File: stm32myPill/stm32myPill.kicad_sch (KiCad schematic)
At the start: 10 parts

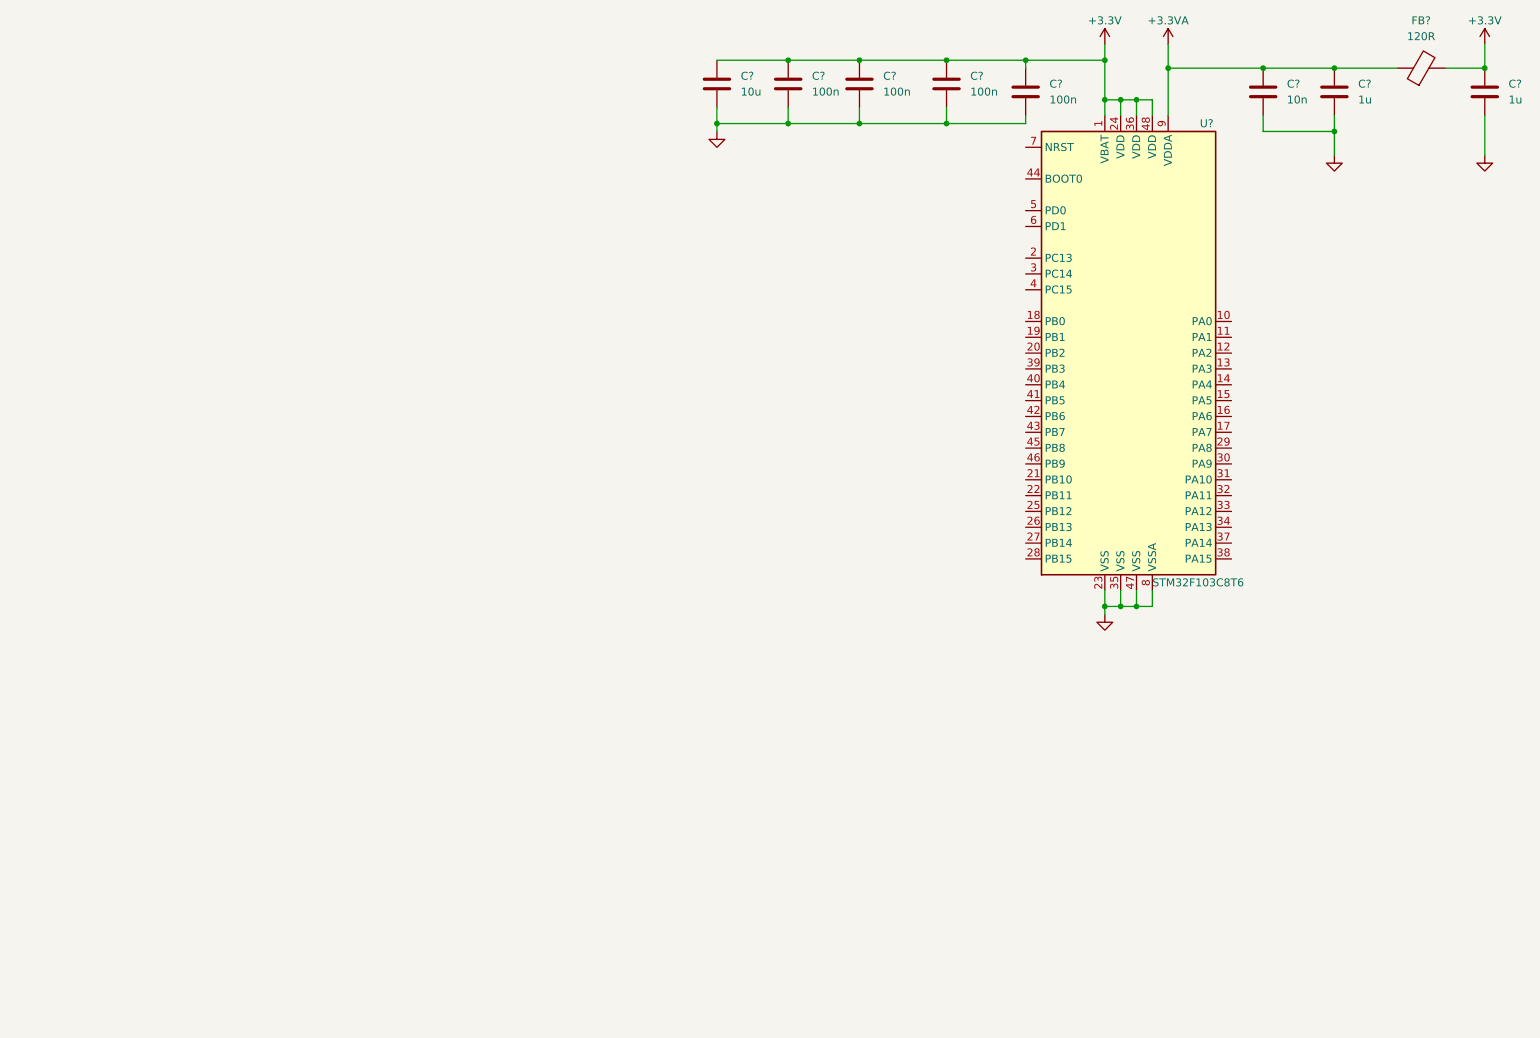
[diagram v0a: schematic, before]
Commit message: added CubeIDE and finished MCU schematic
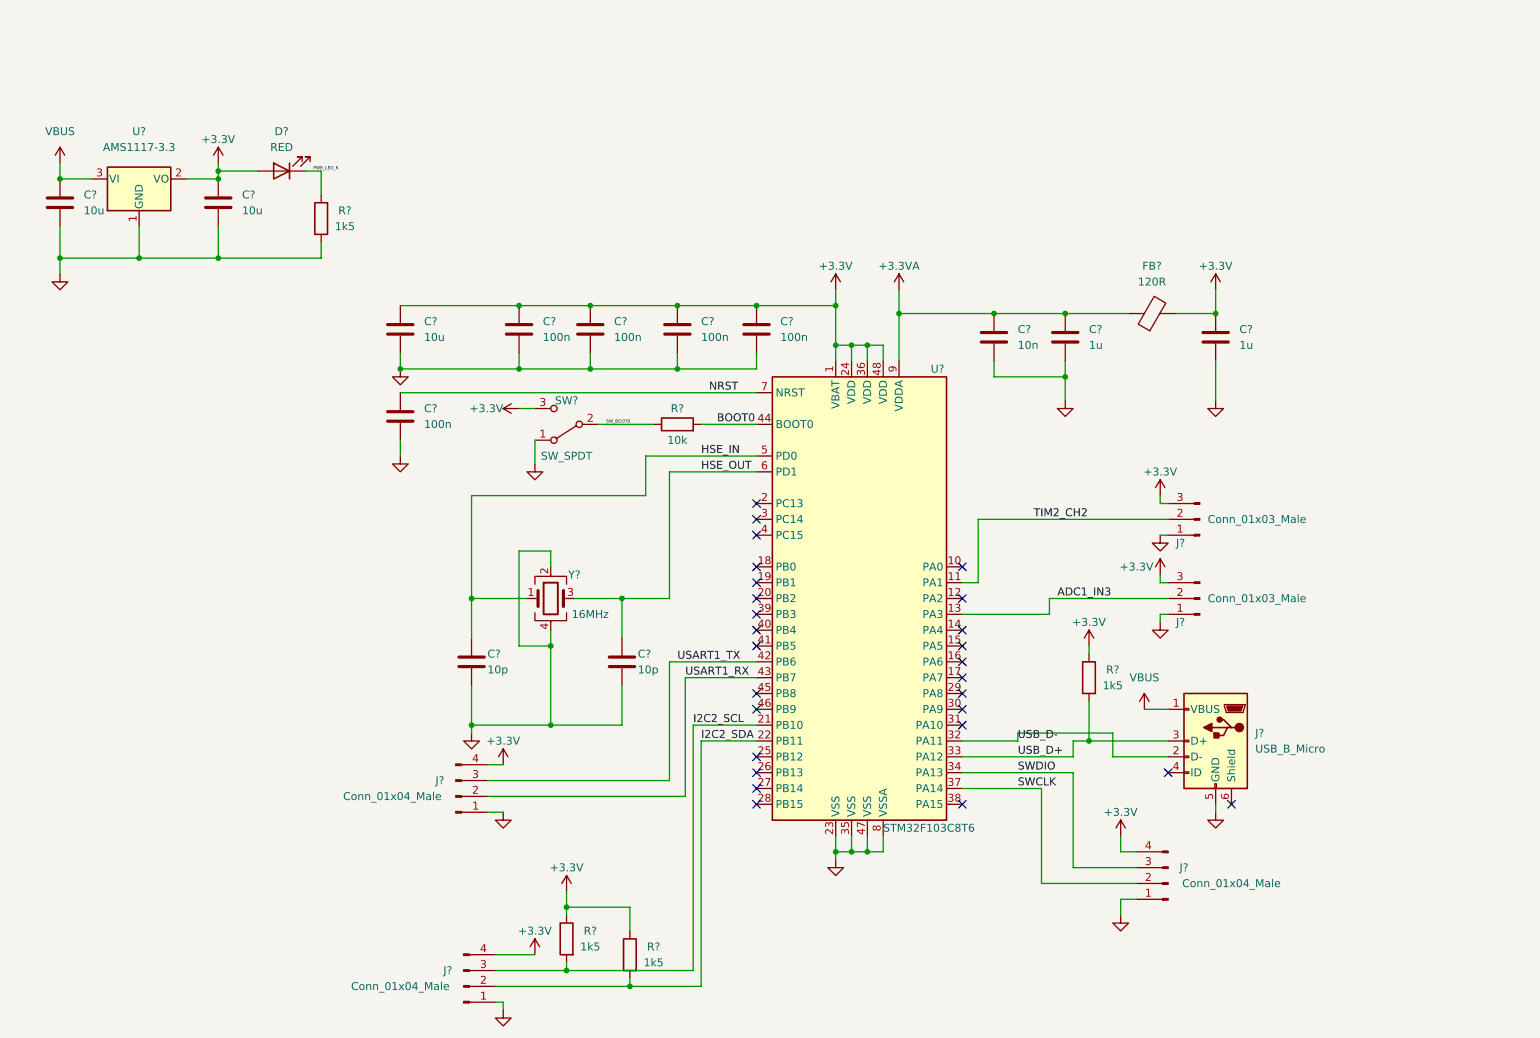
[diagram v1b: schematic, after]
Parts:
- added C? (x2): 10p, symbol Device:C
- added C? (x2): 10u, symbol Device:C
- added C?: 100n, symbol Device:C
- added D?: RED, symbol Device:LED
- added J? (x3): Conn_01x04_Male, symbol Connector:Conn_01x04_Male
- added J? (x2): Conn_01x03_Male, symbol Connector:Conn_01x03_Male
- added J?: USB_B_Micro, symbol Connector:USB_B_Micro
- added R? (x4): 1k5, symbol Device:R
- added R?: 10k, symbol Device:R
- added SW?: SW_SPDT, symbol Switch:SW_SPDT
- added U?: AMS1117-3.3, Package_TO_SOT_SMD:SOT-223-3_TabPin2, symbol Regulator_Linear:AMS1117-3.3
- added Y?: 16MHz, symbol Device:Crystal_GND24
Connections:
- net +3V3: now also C?.1, D?.2 (A), J?.3 (Pin_3), J?.3 (Pin_3), J?.4 (Pin_4), J?.4 (Pin_4), J?.4 (Pin_4), R?.1, R?.1, R?.1, SW?.3 (C), U?.2 (VO)
- net GND: now also C?.2, C?.2, C?.2, C?.2, C?.2, J?.1 (Pin_1), J?.1 (Pin_1), J?.1 (Pin_1), J?.1 (Pin_1), J?.1 (Pin_1), J?.5 (GND), R?.1, SW?.1 (A), U?.1 (GND), Y?.2, Y?.4
- net TIM2_CH2: now reaches U?.11 (PA1)
- net TIM2_CH2: now also J?.2 (Pin_2)
- net ADC1_IN3: now reaches U?.13 (PA3)
- net ADC1_IN3: now also J?.2 (Pin_2)
- net I2C2_SCL: now reaches U?.21 (PB10)
- net I2C2_SCL: now also J?.3 (Pin_3), R?.2
- net I2C2_SDA: now reaches U?.22 (PB11)
- net I2C2_SDA: now also J?.2 (Pin_2), R?.2
- net USB_D-: now reaches U?.32 (PA11)
- net USB_D-: now also J?.2 (D-)
- net USB_D+: now reaches U?.33 (PA12)
- net USB_D+: now also J?.3 (D+), R?.2
- net SWDIO: now reaches U?.34 (PA13)
- net SWDIO: now also J?.3 (Pin_3)
- net SWCLK: now reaches U?.37 (PA14)
- net SWCLK: now also J?.2 (Pin_2)
- net USART1_TX: now reaches U?.42 (PB6)
- net USART1_TX: now also J?.3 (Pin_3)
- net USART1_RX: now reaches U?.43 (PB7)
- net USART1_RX: now also J?.2 (Pin_2)
- net BOOT0: now reaches U?.44 (BOOT0)
- net BOOT0: now also R?.2
- net HSE_IN: now reaches U?.5 (PD0)
- net HSE_IN: now also C?.1, Y?.1
- net HSE_OUT: now reaches U?.6 (PD1)
- net HSE_OUT: now also C?.1, Y?.3
- net NRST: now reaches U?.7 (NRST)
- net NRST: now also C?.1
- new net PWR_LED_K: D?.1 (K), R?.2
- new net SW_BOOT0: R?.1, SW?.2 (B)
- new net VBUS: C?.1, J?.1 (VBUS), U?.3 (VI)
- no-connect marks 0 -> 27
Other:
- moved on the sheet: C?, FB?, U?

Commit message: completed sch and added footprints
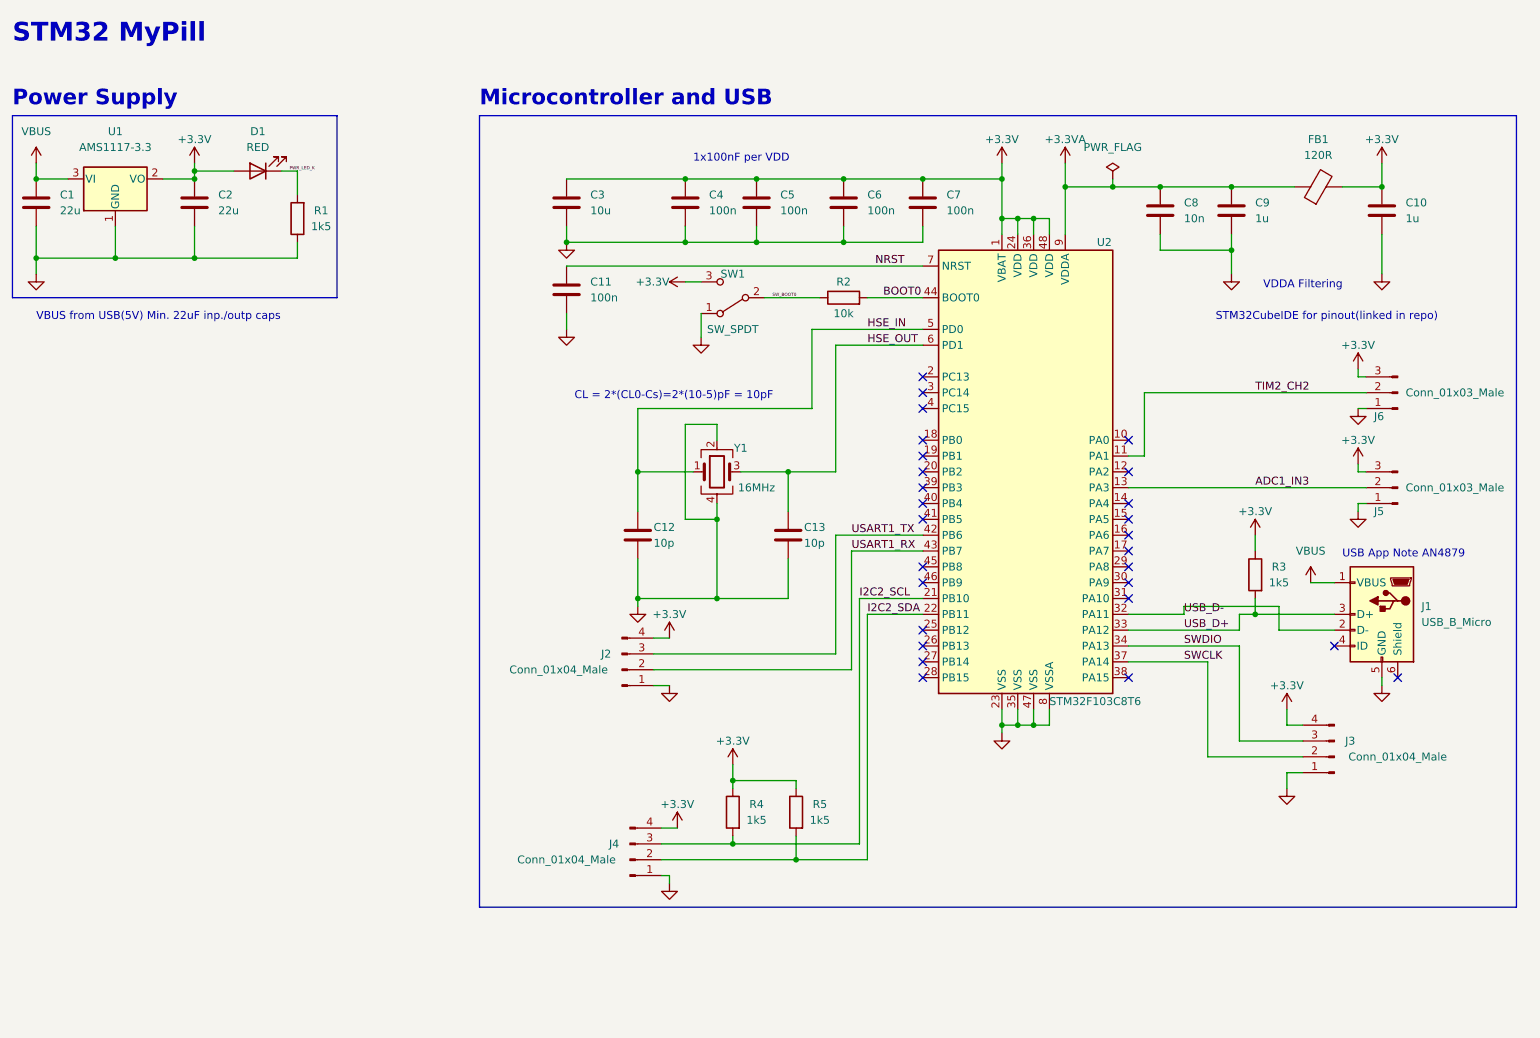
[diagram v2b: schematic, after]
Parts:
- C1, C2: renamed from C?; value 10u -> 22u; footprint (none) -> Capacitor_SMD:C_0805_2012Metric
- C10, C11, C12, C13, C4, C5, C6, C7, C8, C9: renamed from C?; footprint (none) -> Capacitor_SMD:C_0402_1005Metric
- C3: renamed from C?; footprint (none) -> Capacitor_SMD:C_0603_1608Metric
- D1: renamed from D?; footprint (none) -> LED_SMD:LED_0603_1608Metric
- FB1: renamed from FB?; footprint (none) -> Inductor_SMD:L_0603_1608Metric
- J1: renamed from J?; footprint (none) -> Connector_USB:USB_Micro-B_Wuerth_629105150521
- J2, J3, J4: renamed from J?; footprint (none) -> Connector_PinHeader_2.54mm:PinHeader_1x04_P2.54mm_Vertical
- J5, J6: renamed from J?; footprint (none) -> Connector_PinHeader_2.54mm:PinHeader_1x03_P2.54mm_Vertical
- R1, R2, R3, R4, R5: renamed from R?; footprint (none) -> Resistor_SMD:R_0402_1005Metric
- SW1: renamed from SW?; footprint (none) -> Button_Switch_THT:SW_E-Switch_EG1224_SPDT_Angled
- Y1: renamed from Y?; footprint (none) -> Crystal:Crystal_SMD_3225-4Pin_3.2x2.5mm
- gave numbers to parts that had none: 2
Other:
- note added: "1x100nF per VDD"
- note added: "CL = 2*(CL0-Cs)=2*(10-5)pF = 10pF"
- note added: "Microcontroller and USB"
- note added: "Power Supply"
- note added: "STM32 MyPill"
- note added: "STM32CubeIDE for pinout(linked in repo)"
- note added: "USB App Note AN4879"
- note added: "VBUS from USB(5V) Min. 22uF inp./outp caps"
- note added: "VDDA Filtering"
- company: (none) -> Suri Labs 
- title: (none) -> STM32 MyPill
- moved on the sheet: C1, C10, C11, C12, C13, C2, C3, C4, C5, C6, C7, C8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

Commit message: finished layout added mounting holes
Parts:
- removed J5, J6: Conn_01x03_Male, Connector_PinHeader_2.54mm:PinHeader_1x03_P2.54mm_Vertical, symbol Connector:Conn_01x03_Male
- added H1, H2, H3, H4: MountingHole, MountingHole:MountingHole_2.2mm_M2, symbol Mechanical:MountingHole
- SW1: footprint Button_Switch_THT:SW_E-Switch_EG1224_SPDT_Angled -> Button_Switch_SMD:SW_SPDT_PCM12
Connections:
- net ADC1_IN3: no longer names the net of U2.13 (PA3)
- net TIM2_CH2: no longer names the net of U2.11 (PA1)
- no-connect marks 27 -> 29
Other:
- note added: "M2 Screw"
- note added: "Mounting Holes"
- note added: "Pull-Up for I2C"
